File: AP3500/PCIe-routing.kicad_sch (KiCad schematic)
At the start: 14 parts, among them J12 Bus_PCI_Express_Mini

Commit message: More work on Antennas - laying out the new panel as a 2x2 aperture coupled patch
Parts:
- C23, C3, C39, C40, C43, C44: value .1u 25v -> 100n 50v; LCSC (none) -> C14663; PartsBoxID 0603-100nF-X7R-25V -> 0603-100nF-X7R-50V
- C41, C42: LCSC (none) -> C96123
- R57: LCSC (none) -> C23162
- R61: value 0 1% -> 0R 1%; LCSC (none) -> C21189
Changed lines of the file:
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@@
-(kicad_sch (version 20201015) (generator eeschema)
+(kicad_sch (version 20210126) (generator eeschema)
   (paper "A4")
   (title_block
@@
       (effects (font (size 1.27 1.27)) hide)
     )
+    (pin "1")
   )
   (symbol (lib_id "power:GND") (at 51.435 46.99 0) (unit 1)
@@
       (effects (font (size 1.27 1.27)) hide)
     )
+    (pin "1")
   )
   (symbol (lib_id "power:GND") (at 111.76 105.41 0) (unit 1)
@@
       (effects (font (size 1.27 1.27)) hide)
     )
+    (pin "1")
   )
   (symbol (lib_id "power:GND") (at 153.035 80.645 0) (unit 1)
@@
       (effects (font (size 1.27 1.27)) hide)
     )
+    (pin "1")
   )
   (symbol (lib_id "Device:R") (at 61.595 102.235 0) (mirror x) (unit 1)
@@
       (effects (font (size 1.27 1.27)) hide)
     )
+    (pin "1")
+    (pin "2")
   )
   (symbol (lib_id "Device:R") (at 62.865 87.63 180) (unit 1)
@@
       (effects (font (size 1.27 1.27)) hide)
     )
+    (pin "1")
+    (pin "2")
   )
   (symbol (lib_id "Device:R") (at 83.82 90.17 270) (mirror x) (unit 1)
@@
       (effects (font (size 1.27 1.27)) hide)
     )
+    (property "LCSC" "C23162" (id 4) (at 83.82 90.17 0)
+      (effects (font (size 1.27 1.27)) hide)
+    )
+    (pin "1")
+    (pin "2")
   )
   (symbol (lib_id "Device:R") (at 84.455 97.79 270) (mirror x) (unit 1)
@@
       (effects (font (size 1.27 1.27)) (justify left))
     )
-    (property "Value" "0 1%" (id 1) (at 87.122 96.52 90)
+    (property "Value" "0R 1%" (id 1) (at 87.122 96.52 90)
       (effects (font (size 1.27 1.27)) (justify left))
     )
@@
       (effects (font (size 1.27 1.27)) hide)
     )
+    (property "LCSC" "C21189" (id 4) (at 84.455 97.79 0)
+      (effects (font (size 1.27 1.27)) hide)
+    )
+    (pin "1")
+    (pin "2")
   )
   (symbol (lib_id "Jumper:Jumper_2_Open") (at 146.05 69.85 0) (unit 1)
@@
       (effects (font (size 1.27 1.27)) hide)
     )
+    (pin "1")
+    (pin "2")
   )
   (symbol (lib_id "Device:C") (at 30.48 40.005 0) (unit 1)
@@
       (effects (font (size 1.27 1.27)) (justify left))
     )
-    (property "Value" ".1u 25v" (id 1) (at 27.051 44.958 0)
+    (property "Value" "100n 50v" (id 1) (at 27.051 44.958 0)
       (effects (font (size 1.27 1.27)) (justify left))
     )
@@
       (effects (font (size 1.27 1.27)) hide)
     )
-    (property "PartsBoxID" "0603-100nF-X7R-25V" (id 4) (at 30.48 40.005 0)
-      (effects (font (size 1.27 1.27)) hide)
-    )
+    (property "PartsBoxID" "0603-100nF-X7R-50V" (id 4) (at 30.48 40.005 0)
+      (effects (font (size 1.27 1.27)) hide)
+    )
+    (property "LCSC" "C14663" (id 4) (at 30.48 40.005 0)
+      (effects (font (size 1.27 1.27)) hide)
+    )
+    (pin "1")
+    (pin "2")
   )
   (symbol (lib_id "Device:C") (at 38.1 40.005 0) (unit 1)
@@
       (effects (font (size 1.27 1.27)) (justify left))
     )
-    (property "Value" ".1u 25v" (id 1) (at 34.671 44.958 0)
+    (property "Value" "100n 50v" (id 1) (at 34.671 44.958 0)
       (effects (font (size 1.27 1.27)) (justify left))
     )
@@
       (effects (font (size 1.27 1.27)) hide)
     )
-    (property "PartsBoxID" "0603-100nF-X7R-25V" (id 4) (at 38.1 40.005 0)
-      (effects (font (size 1.27 1.27)) hide)
-    )
+    (property "PartsBoxID" "0603-100nF-X7R-50V" (id 4) (at 38.1 40.005 0)
+      (effects (font (size 1.27 1.27)) hide)
+    )
+    (property "LCSC" "C14663" (id 4) (at 38.1 40.005 0)
+      (effects (font (size 1.27 1.27)) hide)
+    )
+    (pin "1")
+    (pin "2")
   )
   (symbol (lib_id "Device:C") (at 51.435 40.005 0) (unit 1)
@@
       (effects (font (size 1.27 1.27)) (justify left))
     )
-    (property "Value" ".1u 25v" (id 1) (at 48.006 44.958 0)
+    (property "Value" "100n 50v" (id 1) (at 48.006 44.958 0)
       (effects (font (size 1.27 1.27)) (justify left))
     )
@@
       (effects (font (size 1.27 1.27)) hide)
     )
-    (property "PartsBoxID" "0603-100nF-X7R-25V" (id 4) (at 51.435 40.005 0)
-      (effects (font (size 1.27 1.27)) hide)
-    )
+    (property "PartsBoxID" "0603-100nF-X7R-50V" (id 4) (at 51.435 40.005 0)
+      (effects (font (size 1.27 1.27)) hide)
+    )
+    (property "LCSC" "C14663" (id 4) (at 51.435 40.005 0)
+      (effects (font (size 1.27 1.27)) hide)
+    )
+    (pin "1")
+    (pin "2")
   )
   (symbol (lib_id "Device:C") (at 59.055 40.005 0) (unit 1)
@@
       (effects (font (size 1.27 1.27)) (justify left))
     )
-    (property "Value" ".1u 25v" (id 1) (at 55.626 44.958 0)
+    (property "Value" "100n 50v" (id 1) (at 55.626 44.958 0)
       (effects (font (size 1.27 1.27)) (justify left))
     )
@@
       (effects (font (size 1.27 1.27)) hide)
     )
-    (property "PartsBoxID" "0603-100nF-X7R-25V" (id 4) (at 59.055 40.005 0)
-      (effects (font (size 1.27 1.27)) hide)
-    )
+    (property "PartsBoxID" "0603-100nF-X7R-50V" (id 4) (at 59.055 40.005 0)
+      (effects (font (size 1.27 1.27)) hide)
+    )
+    (property "LCSC" "C14663" (id 4) (at 59.055 40.005 0)
+      (effects (font (size 1.27 1.27)) hide)
+    )
+    (pin "1")
+    (pin "2")
   )
   (symbol (lib_id "Device:C") (at 153.035 74.93 0) (unit 1)
@@
       (effects (font (size 1.27 1.27)) hide)
     )
+    (property "LCSC" "C96123" (id 4) (at 153.035 74.93 0)
+      (effects (font (size 1.27 1.27)) hide)
+    )
+    (pin "1")
+    (pin "2")
   )
   (symbol (lib_id "Device:C") (at 161.925 74.93 0) (unit 1)
@@
       (effects (font (size 1.27 1.27)) hide)
     )
+    (property "LCSC" "C96123" (id 4) (at 161.925 74.93 0)
+      (effects (font (size 1.27 1.27)) hide)
+    )
+    (pin "1")
+    (pin "2")
   )
   (symbol (lib_id "Device:C") (at 169.545 74.93 0) (unit 1)
@@
       (effects (font (size 1.27 1.27)) (justify left))
     )
-    (property "Value" ".1u 25v" (id 1) (at 166.116 79.248 0)
+    (property "Value" "100n 50v" (id 1) (at 166.116 79.248 0)
       (effects (font (size 1.27 1.27)) (justify left))
     )
@@
       (effects (font (size 1.27 1.27)) hide)
     )
-    (property "PartsBoxID" "0603-100nF-X7R-25V" (id 4) (at 169.545 74.93 0)
-      (effects (font (size 1.27 1.27)) hide)
-    )
+    (property "PartsBoxID" "0603-100nF-X7R-50V" (id 4) (at 169.545 74.93 0)
+      (effects (font (size 1.27 1.27)) hide)
+    )
+    (property "LCSC" "C14663" (id 4) (at 169.545 74.93 0)
+      (effects (font (size 1.27 1.27)) hide)
+    )
+    (pin "1")
+    (pin "2")
   )
   (symbol (lib_id "Device:C") (at 177.165 74.93 0) (unit 1)
@@
       (effects (font (size 1.27 1.27)) (justify left))
     )
-    (property "Value" ".1u 25v" (id 1) (at 173.736 79.248 0)
+    (property "Value" "100n 50v" (id 1) (at 173.736 79.248 0)
       (effects (font (size 1.27 1.27)) (justify left))
     )
@@
       (effects (font (size 1.27 1.27)) hide)
     )
-    (property "PartsBoxID" "0603-100nF-X7R-25V" (id 4) (at 177.165 74.93 0)
-      (effects (font (size 1.27 1.27)) hide)
-    )
+    (property "PartsBoxID" "0603-100nF-X7R-50V" (id 4) (at 177.165 74.93 0)
+      (effects (font (size 1.27 1.27)) hide)
+    )
+    (property "LCSC" "C14663" (id 4) (at 177.165 74.93 0)
+      (effects (font (size 1.27 1.27)) hide)
+    )
+    (pin "1")
+    (pin "2")
   )
   (symbol (lib_id "Connector:Bus_PCI_Express_Mini") (at 111.76 72.39 0) (unit 1)
@@
       (effects (font (size 1.27 1.27)) hide)
     )
+    (pin "1")
+    (pin "10")
+    (pin "11")
+    (pin "12")
+    (pin "13")
+    (pin "14")
+    (pin "15")
+    (pin "16")
+    (pin "17")
+    (pin "18")
+    (pin "19")
+    (pin "2")
+    (pin "20")
+    (pin "21")
+    (pin "22")
+    (pin "23")
+    (pin "24")
+    (pin "25")
+    (pin "26")
+    (pin "27")
+    (pin "28")
+    (pin "29")
+    (pin "3")
+    (pin "30")
+    (pin "31")
+    (pin "32")
+    (pin "33")
+    (pin "34")
+    (pin "35")
+    (pin "36")
+    (pin "37")
+    (pin "38")
+    (pin "39")
+    (pin "4")
+    (pin "40")
+    (pin "41")
+    (pin "42")
+    (pin "43")
+    (pin "44")
+    (pin "45")
+    (pin "46")
+    (pin "47")
+    (pin "48")
+    (pin "49")
+    (pin "5")
+    (pin "50")
+    (pin "51")
+    (pin "52")
+    (pin "6")
+    (pin "7")
+    (pin "8")
+    (pin "9")
+    (pin "MP")
   )
 )

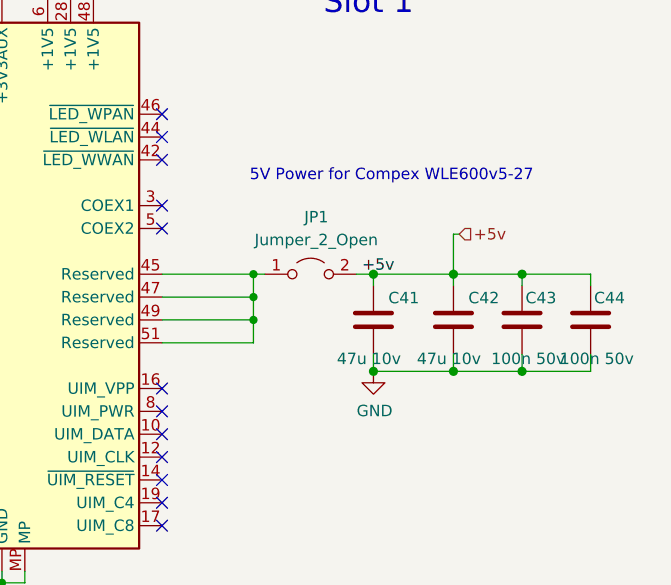
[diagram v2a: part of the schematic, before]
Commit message: Add new single polarity aperture coupled 4x4 antenna. RasPiCNM4Connector test Gerbers for PCBWay Cleanups and optimixations for AP3500
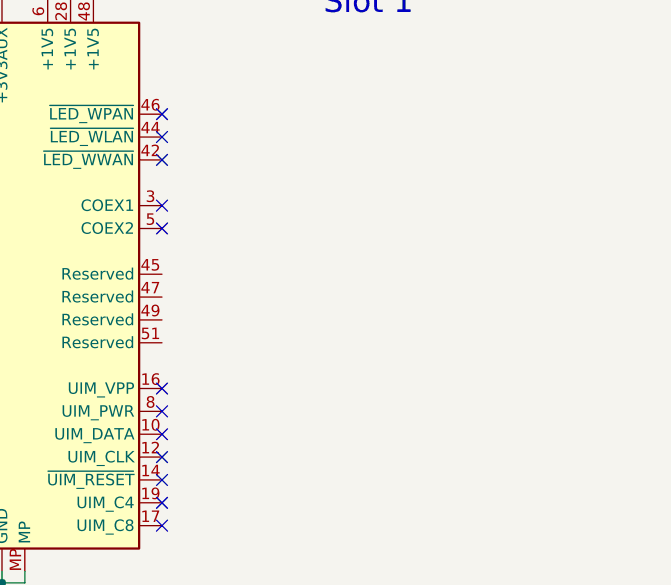
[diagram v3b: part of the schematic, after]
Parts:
- removed C41, C42: 47u 10v, Capacitor_SMD:C_1206_3216Metric, symbol Device:C
- removed C43, C44: 100n 50v, Capacitor_SMD:C_0603_1608Metric, symbol Device:C
- removed JP1: Jumper_2_Open, Connector_PinHeader_2.54mm:PinHeader_1x02_P2.54mm_Vertical, symbol Jumper:Jumper_2_Open
- C23, C3, C39, C40: PartsBoxID 0603-100nF-X7R-50V -> (none)
- R61: PartsBoxID 0603-0R-1% -> (none)
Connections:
- now unconnected: J12.45 (Reserved), J12.47 (Reserved), J12.49 (Reserved), J12.51 (Reserved)
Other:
- note removed: "5V Power for Compex WLE600v5-27"

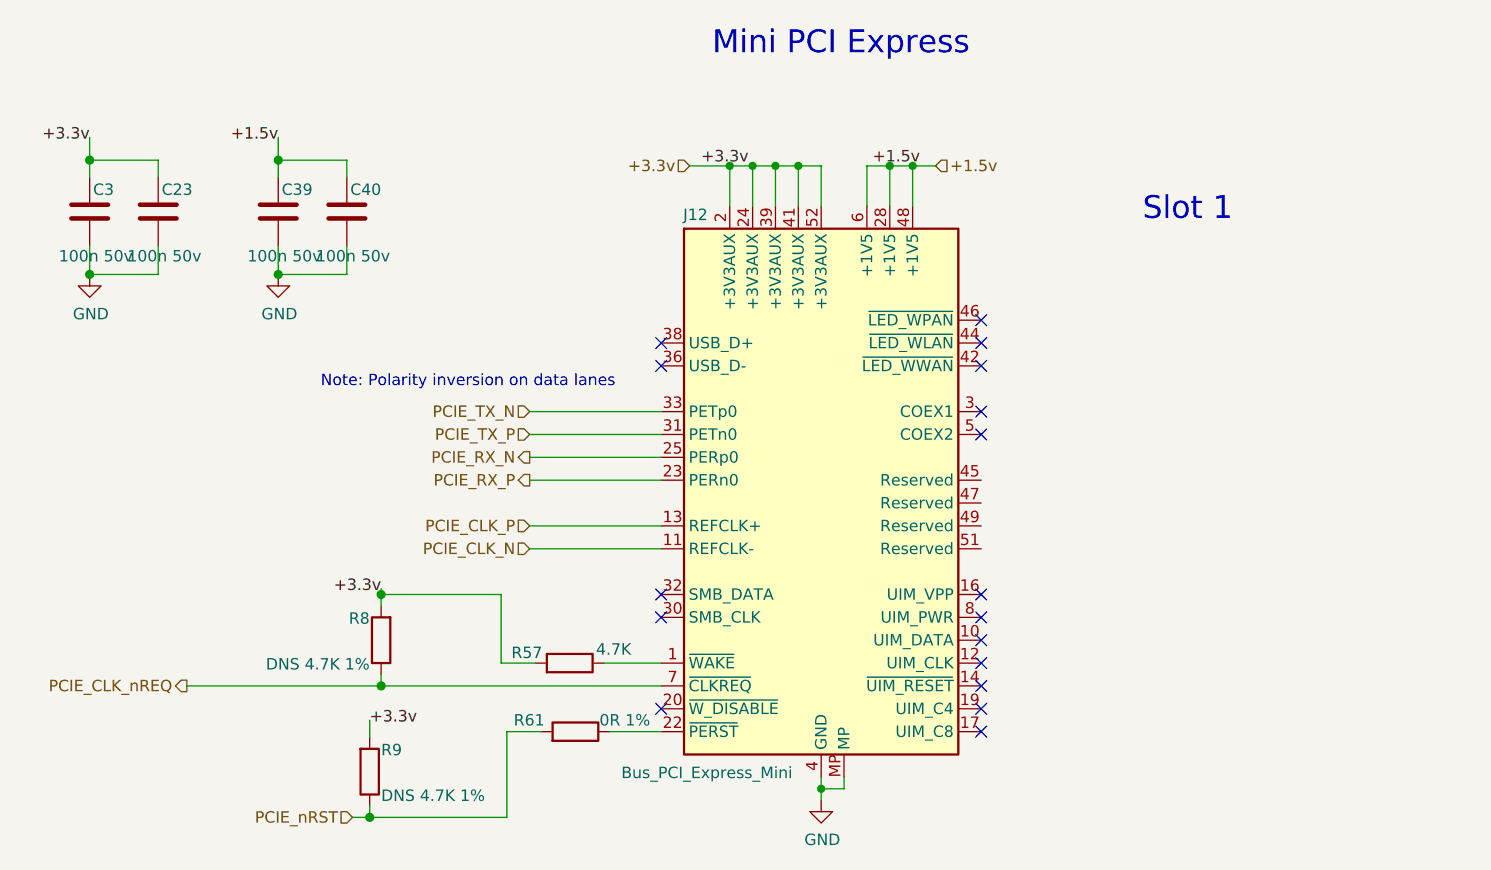
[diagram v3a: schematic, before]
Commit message: Updates for JLCPCB components actually in stock at this time
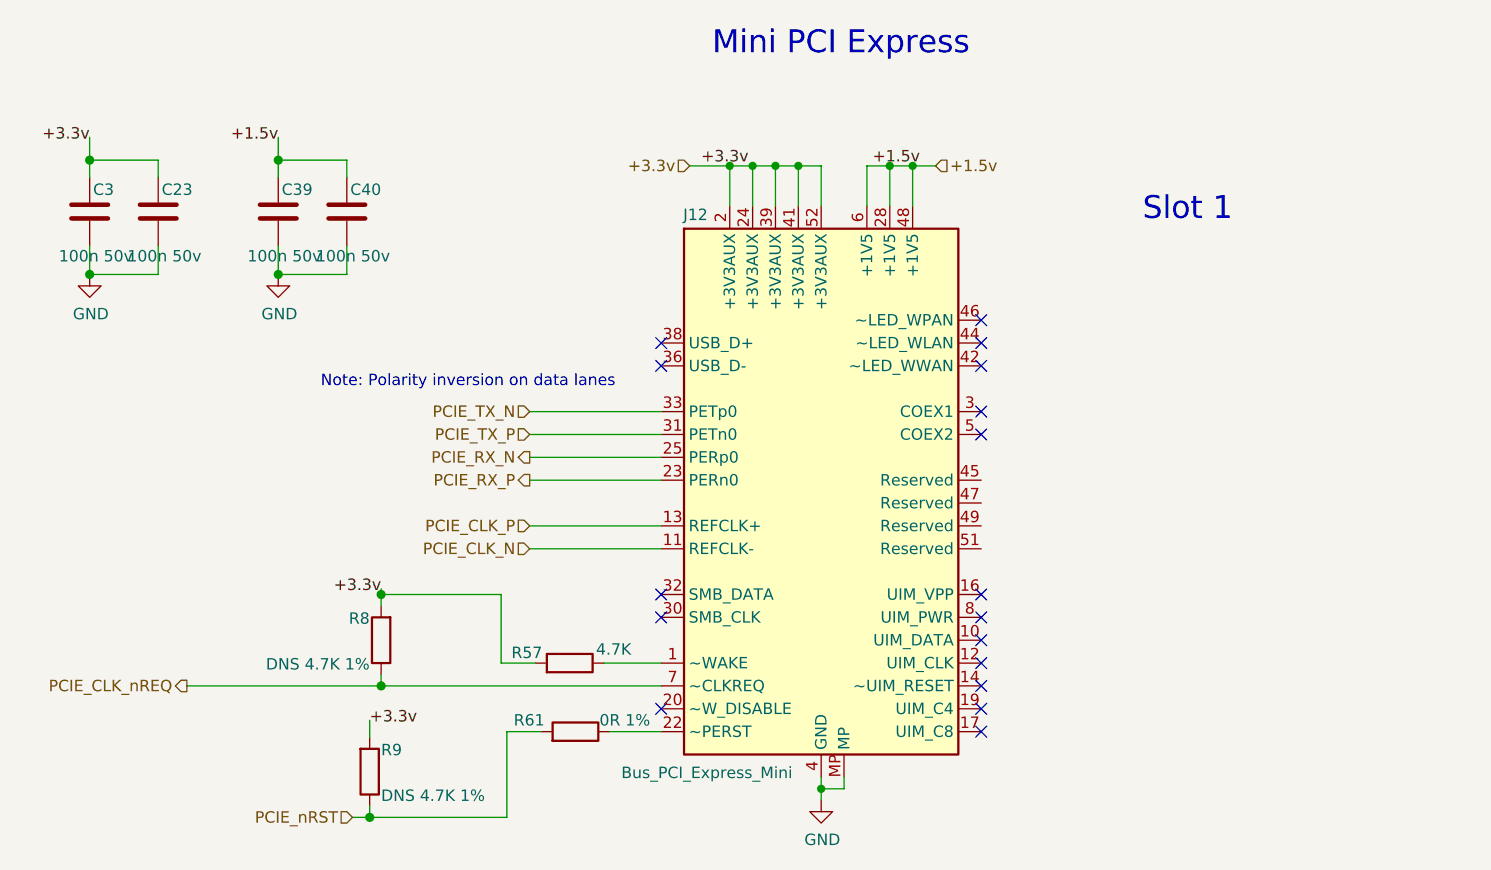
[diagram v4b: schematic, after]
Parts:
- J12: LCSC (none) -> C404121
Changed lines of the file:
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@@
-(kicad_sch (version 20210406) (generator eeschema)
+(kicad_sch (version 20210606) (generator eeschema)
   (paper "A4")
   (title_block
@@
       (effects (font (size 1.27 1.27)) hide)
     )
+    (property "LCSC" "C404121" (id 10) (at 111.76 72.39 0)
+      (effects (font (size 1.27 1.27)) hide)
+    )
